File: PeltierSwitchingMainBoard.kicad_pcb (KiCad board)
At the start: 2 copper layers, 52 parts, among them J1 +12VIn, J10 Conn_01x02, J11 Conn_01x02, J2 GNDIn, J3 Molex Micro Lock (1.25mm 1.5A), J4 Conn_01x02, J5 Conn_01x02, J6 Conn_01x02, J7 Conn_01x02, J8 Conn_01x02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

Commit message: Almost finalized designing single board
Signed-off-by: bebenlebricolo <benoittarrade@hotmail.fr>
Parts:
- added H1: MountingHole_Pad, MountingHole:MountingHole_4mm_Pad_TopOnly, F.Cu at (252.7, 127.0)
- added H2: MountingHole_Pad, MountingHole:MountingHole_4mm_Pad_TopOnly, F.Cu at (166.4, 127.0)
- added H3: MountingHole_Pad, MountingHole:MountingHole_4mm_Pad_TopOnly, F.Cu at (252.7, 47.0)
- added H4: MountingHole_Pad, MountingHole:MountingHole_4mm_Pad_TopOnly, F.Cu at (166.4, 47.0)
- added R12: 0, Resistor_SMD:R_2512_6332Metric_Pad1.40x3.35mm_HandSolder, F.Cu at (200.2, 126.0)
- added R13: 0, Resistor_SMD:R_1206_3216Metric_Pad1.30x1.75mm_HandSolder, F.Cu at (179.8, 93.0)
- added R14: 0, Resistor_SMD:R_1206_3216Metric_Pad1.30x1.75mm_HandSolder, F.Cu at (171.7, 90.4)
- added R15: 0, Resistor_SMD:R_1206_3216Metric_Pad1.30x1.75mm_HandSolder, F.Cu at (175.8, 94.5)
- added R16: 0, Resistor_SMD:R_1206_3216Metric_Pad1.30x1.75mm_HandSolder, F.Cu at (171.7, 93.0)
- added R17: 0, Resistor_SMD:R_1206_3216Metric_Pad1.30x1.75mm_HandSolder, F.Cu at (171.2, 103.1)
- added R18: 0, Resistor_SMD:R_2512_6332Metric_Pad1.40x3.35mm_HandSolder, F.Cu at (170.2, 97.0)
- added R19: 0, Resistor_SMD:R_2512_6332Metric_Pad1.40x3.35mm_HandSolder, F.Cu at (173.2, 109.2)
- added R20: 0, Resistor_SMD:R_1206_3216Metric_Pad1.30x1.75mm_HandSolder, F.Cu at (168.1, 85.9)
- U2, U3, U4, U5: footprint STD80N6F6:STD80N6F6 -> Package_TO_SOT_SMD:TO-252-2
- moved C6 177.8 mm to (248.9, 62.0)
- moved C2 172.6 mm to (248.9, 58.9)
- moved J2 166.9 mm to (232.9, 128.3), turned to 270 degrees
- moved R10 148.8 mm to (232.6, 51.3), turned to 180 degrees
- moved J11 137.2 mm to (229.6, 90.2)
- moved R9 137.0 mm to (208.3, 128.9), turned to 270 degrees
- moved J1 128.8 mm to (224.3, 45.7), turned to 90 degrees
- moved C4 125.6 mm to (247.9, 70.1)
- moved J5 122.7 mm to (229.6, 105.2)
- moved R11 122.1 mm to (214.9, 116.8), turned to 180 degrees
- moved J10 120.7 mm to (229.1, 62.0)
- moved L2 119.8 mm to (198.1, 113.0)
- moved TP1 109.0 mm to (231.1, 55.9)
- moved C5 105.7 mm to (247.9, 81.8)
- moved J7 105.4 mm to (229.1, 74.7)
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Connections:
- C10 pad 1: /ALS -> /VSense
- C11 pad 1: /ALS -> /VSense
- C9 pad 1: /ALS -> Net-(C9-Pad1)
- D1 pad 2: +12V -> Net-(D1-Pad2)
- D2 pad 2: +12V -> Net-(D1-Pad2)
- J3 pad 1: /IN+ -> /HEN
- J3 pad 2: /IN- -> /Disable
- J3 pad 3: /Disable -> GND
- J3 pad 4: /HEN -> /IN+
- J3 pad 5: /ALS -> /IN-
- J3 pad 6: Net-(J3-Pad6) -> /VSense
- R7 pad 2: /AHO -> /AHO-gate
- R8 pad 2: /ALO -> /ALO-gate
- R9 pad 1: /ALS -> /VSense
- TP3 pad 1: /ALO -> /ALO-gate
- TP4 pad 1: /AHO -> /AHO-gate
- TP7 pad 1: /ALS -> /VSense
- U1 pad 15: +12V -> Net-(D1-Pad2)
- U1 pad 16: +12V -> Net-(D1-Pad2)
- U1 pad 17: /ALS -> /BLS
- U1 pad 4: GND -> Net-(R20-Pad2)
- U3 pad 3: /ALS -> Net-(C9-Pad1)
- U5 pad 3: /ALS -> /VSense
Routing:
- net /PeltierLeft: track 0.00 -> 209.9 mm
- net /VSense: track 0.00 -> 146.3 mm
- net /PeltierRight: track 0.00 -> 127.3 mm
- net /BHO: track 0.00 -> 99.1 mm
- net Net-(L1-Pad1): track 0.00 -> 72.9 mm
- net /BLO: track 0.00 -> 72.0 mm
- net Net-(C9-Pad1): track 0.00 -> 63.5 mm
- net /AHO-gate: track 0.00 -> 39.0 mm
- net Net-(R6-Pad1): track 0.00 -> 37.4 mm
- net Net-(R5-Pad1): track 0.00 -> 36.7 mm
- net /Disable: track 0.00 -> 36.6 mm
- net /ALO-gate: track 0.00 -> 31.3 mm
- net Net-(D1-Pad2): track 0.00 -> 30.5 mm
- net /HEN: track 0.00 -> 29.9 mm
- net GND: track 0.00 -> 29.1 mm
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- added copper zone on F.Cu, net +12V
- added copper zone on F.Cu, net GND
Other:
- board outline added: 101.6 x 95.3 mm
- net class Power track added: clearance 0.4, trace_width 20, via_dia 0.8, via_drill 0.4

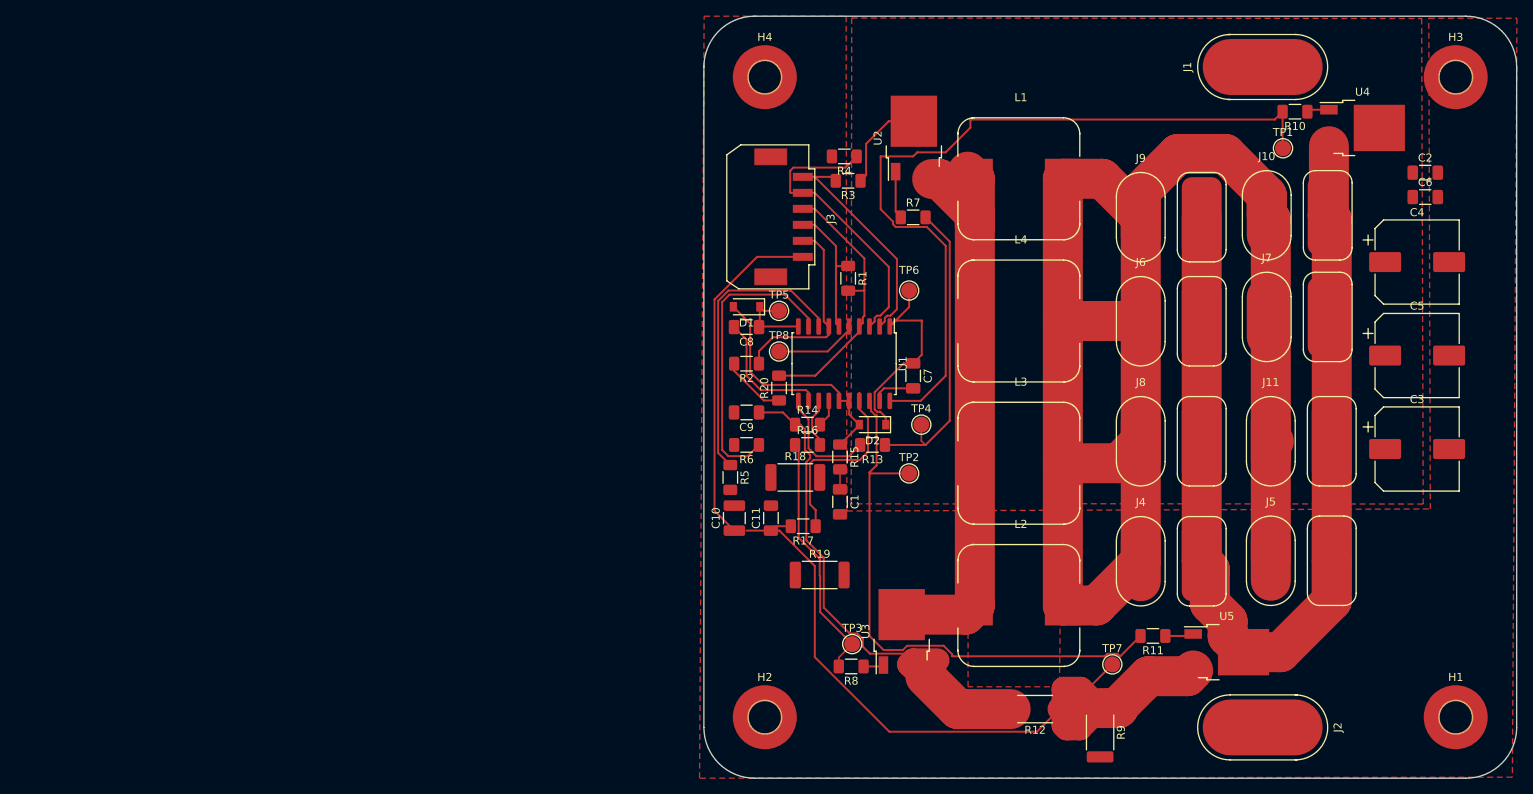
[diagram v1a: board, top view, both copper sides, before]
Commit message: Modified silkscreen and added cooling fans connectors
Signed-off-by: bebenlebricolo <benoittarrade@hotmail.fr>
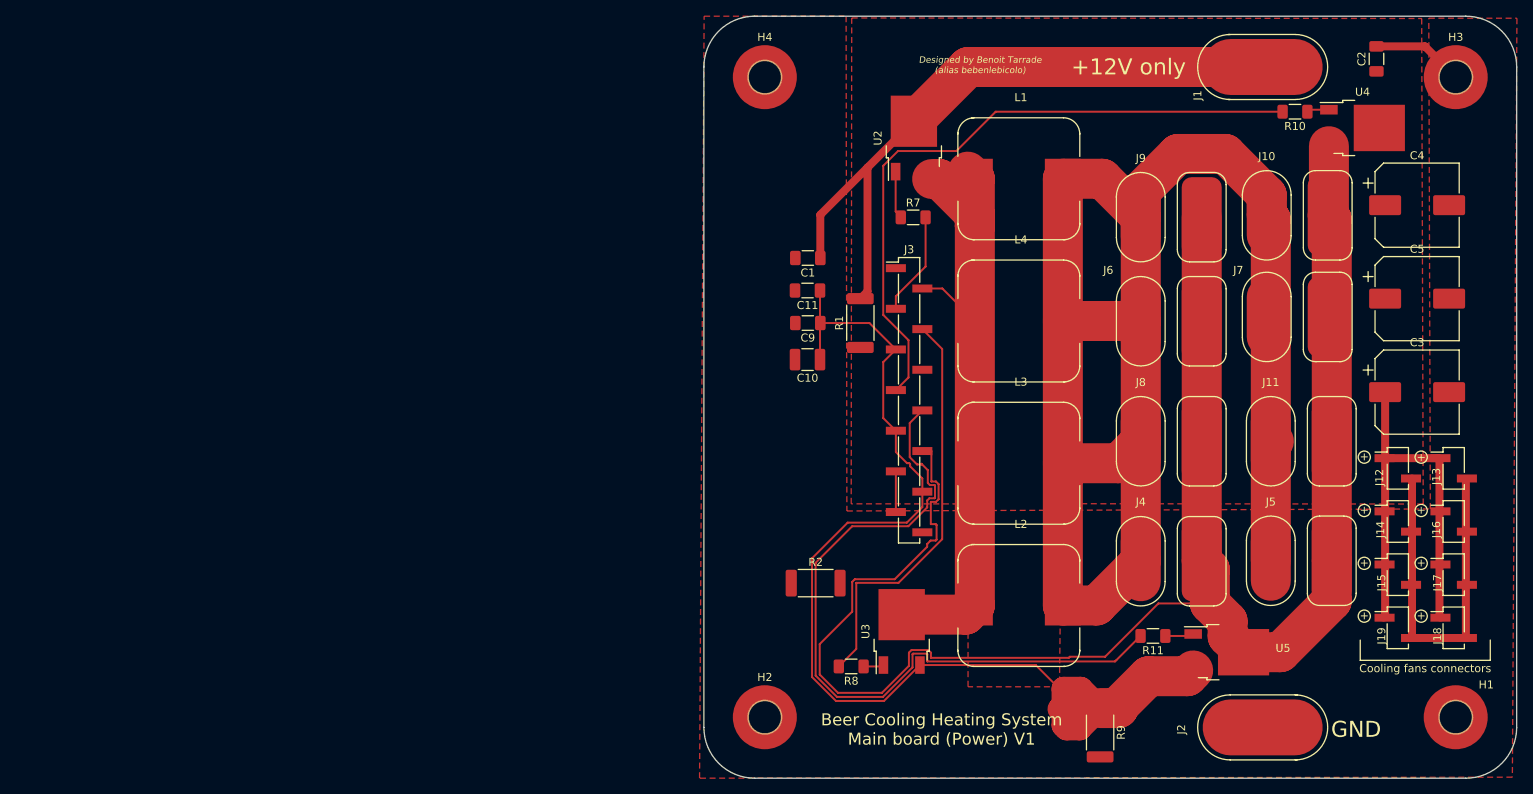
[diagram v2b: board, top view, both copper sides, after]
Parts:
- removed C6: 100nF, Capacitor_SMD:C_1206_3216Metric_Pad1.33x1.80mm_HandSolder
- removed C7, C8: 330nF, Capacitor_SMD:C_1206_3216Metric_Pad1.33x1.80mm_HandSolder
- removed D1, D2: 1N4148W, Diode_SMD:D_SOD-123
- removed R12, R18, R19: 0, Resistor_SMD:R_2512_6332Metric_Pad1.40x3.35mm_HandSolder
- removed R13, R14, R15, R16, R17, R20: 0, Resistor_SMD:R_1206_3216Metric_Pad1.30x1.75mm_HandSolder
- removed R3, R5, R6: 10k, Resistor_SMD:R_1206_3216Metric_Pad1.30x1.75mm_HandSolder
- removed R4: 56k, Resistor_SMD:R_1206_3216Metric_Pad1.30x1.75mm_HandSolder
- removed TP1, TP2, TP3, TP4, TP5, TP6, TP7, TP8: TestPoint, TestPoint:TestPoint_Pad_D2.0mm
- removed U1: HIP4080A, Package_SO:SOIC-20W_7.5x12.8mm_P1.27mm
- added J12: Conn_01x02, Connector_PinHeader_2.54mm:PinHeader_1x02_P2.54mm_Vertical_SMD_Pin1Left, F.Cu at (245.5, 95.9)
- added J13: Conn_01x02, Connector_PinHeader_2.54mm:PinHeader_1x02_P2.54mm_Vertical_SMD_Pin1Left, F.Cu at (252.5, 95.9)
- added J14: Conn_01x02, Connector_PinHeader_2.54mm:PinHeader_1x02_P2.54mm_Vertical_SMD_Pin1Left, F.Cu at (245.5, 102.5)
- added J15: Conn_01x02, Connector_PinHeader_2.54mm:PinHeader_1x02_P2.54mm_Vertical_SMD_Pin1Left, F.Cu at (245.5, 109.2)
- added J16: Conn_01x02, Connector_PinHeader_2.54mm:PinHeader_1x02_P2.54mm_Vertical_SMD_Pin1Left, F.Cu at (252.5, 102.5)
- added J17: Conn_01x02, Connector_PinHeader_2.54mm:PinHeader_1x02_P2.54mm_Vertical_SMD_Pin1Left, F.Cu at (252.5, 109.2)
- added J18: Conn_01x02, Connector_PinHeader_2.54mm:PinHeader_1x02_P2.54mm_Vertical_SMD_Pin1Left, F.Cu at (252.5, 115.8)
- added J19: Conn_01x02, Connector_PinHeader_2.54mm:PinHeader_1x02_P2.54mm_Vertical_SMD_Pin1Left, F.Cu at (245.5, 115.8)
- J3: value Molex Micro Lock (1.25mm 1.5A) -> Conn_01x14; footprint PeltierSwitchingMainBoard:Molex_MicroLock_1.25_01x06 -> Connector_PinHeader_2.54mm:PinHeader_1x14_P2.54mm_Vertical_SMD_Pin1Left
- R1, R2: value 10k -> 0; footprint Resistor_SMD:R_1206_3216Metric_Pad1.30x1.75mm_HandSolder -> Resistor_SMD:R_2512_6332Metric_Pad1.40x3.35mm_HandSolder
- moved J3 32.5 mm to (184.4, 87.4), turned to 0 degrees
- moved C1 30.7 mm to (171.7, 69.6), turned to 180 degrees
- moved C11 28.8 mm to (171.7, 73.7), turned to 180 degrees
- moved R2 28.8 mm to (172.7, 110.2), turned to 0 degrees
- moved C10 21.8 mm to (171.7, 82.3), turned to 180 degrees
- moved C2 15.5 mm to (242.8, 44.7), turned to 90 degrees
- moved C9 13.5 mm to (171.7, 77.7)
- moved C4 7.11 mm to (247.9, 63.0)
- moved C3 7.11 mm to (247.9, 86.4)
- moved C5 7.11 mm to (247.9, 74.7)
- moved R1 5.79 mm to (178.3, 77.7), turned to 90 degrees
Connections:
- C10 pad 1: /VSense -> /ALS
- C11 pad 1: /VSense -> /ALS
- C9 pad 1: Net-(C9-Pad1) -> /ALS
- J10 pad 2: /PeltierRight -> /BHS
- J11 pad 2: /PeltierRight -> /BHS
- J3 pad 1: /HEN -> Net-(J3-Pad1)
- J3 pad 2: /Disable -> /AHS
- J3 pad 3: GND -> /AHO
- J3 pad 4: /IN+ -> /ALO
- J3 pad 5: /IN- -> /ALS
- J3 pad 6: /VSense -> Net-(J3-Pad6)
- J3 pad 7: (no net) -> /BHO
- J4 pad 2: /PeltierRight -> /BHS
- J5 pad 2: /PeltierRight -> /BHS
- J6 pad 2: /PeltierRight -> /BHS
- J7 pad 2: /PeltierRight -> /BHS
- J8 pad 2: /PeltierRight -> /BHS
- J9 pad 2: /PeltierRight -> /BHS
- L1 pad 1: Net-(L1-Pad1) -> /AHS
- L2 pad 1: Net-(L1-Pad1) -> /AHS
- L3 pad 1: Net-(L1-Pad1) -> /AHS
- L4 pad 1: Net-(L1-Pad1) -> /AHS
- R1 pad 1: /IN+ -> +12V
- R1 pad 2: GND -> +12V
- R2 pad 1: /IN- -> GND
- R7 pad 2: /AHO-gate -> /AHO
- R8 pad 2: /ALO-gate -> /ALO
- R9 pad 1: /VSense -> /ALS
- U2 pad 3: Net-(L1-Pad1) -> /AHS
- U3 pad 2: Net-(L1-Pad1) -> /AHS
- U3 pad 3: Net-(C9-Pad1) -> /ALS
- U4 pad 3: /PeltierRight -> /BHS
- U5 pad 2: /PeltierRight -> /BHS
- U5 pad 3: /VSense -> /ALS
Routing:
- net /BHS: track 0.00 -> 224.4 mm
- net /VSense: track 146.3 -> 0.00 mm
- net /ALS: track 3.43 -> 147.7 mm
- net +12V: track 14.6 -> 145.1 mm
- net /PeltierRight: track 127.3 -> 0.00 mm
- net /AHS: track 0.00 -> 81.1 mm
- net Net-(L1-Pad1): track 72.9 -> 0.00 mm
- net Net-(C9-Pad1): track 63.5 -> 0.00 mm
- net /ALO: track 6.25 -> 51.6 mm
- net /AHO-gate: track 39.0 -> 0.00 mm
- net Net-(R6-Pad1): track 37.4 -> 0.00 mm
- net Net-(R5-Pad1): track 36.7 -> 0.00 mm
- net /Disable: track 36.6 -> 0.00 mm
- net /ALO-gate: track 31.3 -> 0.00 mm
- net Net-(D1-Pad2): track 30.5 -> 0.00 mm
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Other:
- board text added: "+"
- board text added: "+12V only"
- board text added: "Beer Cooling Heating System Main board (Power) V1"
- board text added: "Cooling fans connectors"
- board text added: "Designed by Benoit Tarrade (alias bebenlebicolo)"
- board text added: "GND"

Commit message: Updated schematic and silkscreen
Signed-off-by: bebenlebricolo <benoittarrade@hotmail.fr>
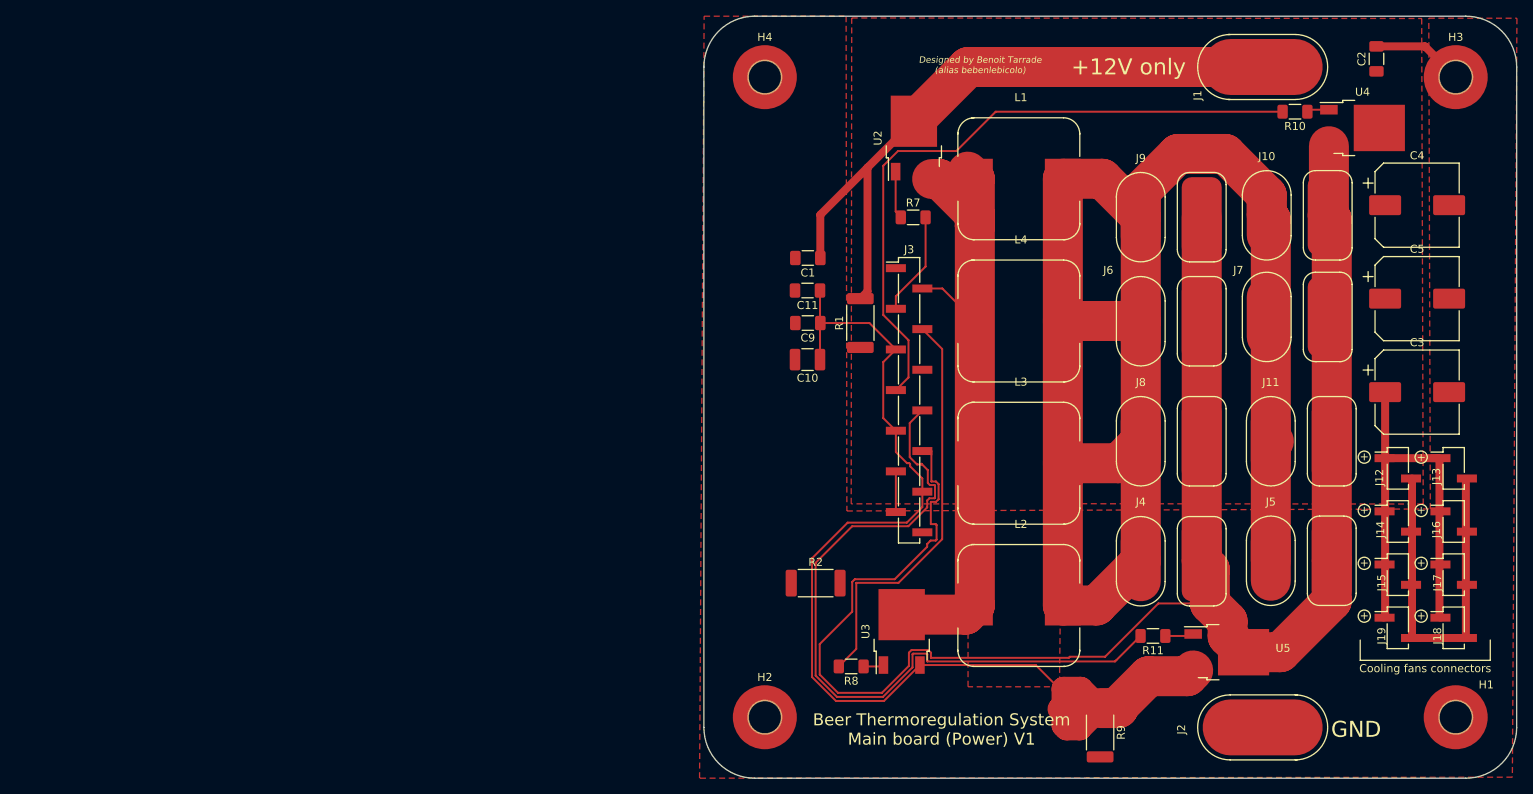
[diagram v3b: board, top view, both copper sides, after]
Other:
- board text added: "Beer Thermoregulation System Main board (Power) V1"
- board text removed: "Beer Cooling Heating System Main board (Power) V1"
